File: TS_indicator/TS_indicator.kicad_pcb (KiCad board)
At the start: 2 copper layers, 140 x 60 mm, 50 parts, among them J1 Conn_01x02_Pin, J2 Conn_01x02_Pin, J3 Conn_01x02_Pin, J4 Conn_01x02_Pin, Q1 AO3401A, Q2 AO3400A, U1 TLV431, U2 PV15-27B12R3, U3 B1212, U7 LTV-817S

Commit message: added TS indicator
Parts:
- F1: footprint Fuse:Fuse_Littelfuse-NANO2-885 -> Fuse:Fuse_Littelfuse-NANO2-462
- moved R9 7.56 mm to (17.4, 36.1)
- moved R8 6.62 mm to (23.5, 36.0)
- moved R7 5.92 mm to (29.5, 35.9)
- moved R6 5.20 mm to (34.4, 37.2), turned to -90 degrees
- moved R10 4.31 mm to (26.2, 44.3), turned to 90 degrees
- moved C1 3.96 mm to (22.6, 52.1)
- moved C2 3.96 mm to (30.6, 49.6)
- moved C3 3.96 mm to (32.4, 63.8)
- moved D1 3.96 mm to (18.0, 47.5)
- moved LM1 3.96 mm to (30.5, 56.2)
- moved R1 3.96 mm to (22.8, 61.0)
- moved R11 3.96 mm to (26.4, 51.0)
- moved R12 3.96 mm to (35.0, 51.3)
- moved R2 3.96 mm to (22.8, 58.5)
- moved R4 3.96 mm to (22.9, 63.6)
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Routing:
- net /Vin: track 23.6 -> 34.5 mm
- net Net-(LM1-+): track 6.23 -> 11.5 mm
- net Net-(LM1-Pad7): track 86.8 -> 83.4 mm
- net Net-(R5-Pad2): track 2.54 -> 5.81 mm
- net /+HV_after_fuse: track 40.1 -> 42.5 mm
- net +12V: track 85.0 -> 83.2 mm
- net Net-(R3-Pad2): track 2.22 -> 3.88 mm
- net Net-(R8-Pad1): track 2.50 -> 3.94 mm
- net GND: track 231.3 -> 232.7 mm
- net /+HV: track 8.73 -> 10.1 mm
- net Net-(R6-Pad1): track 2.64 -> 3.87 mm
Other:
- outline, holes or cut-outs redrawn

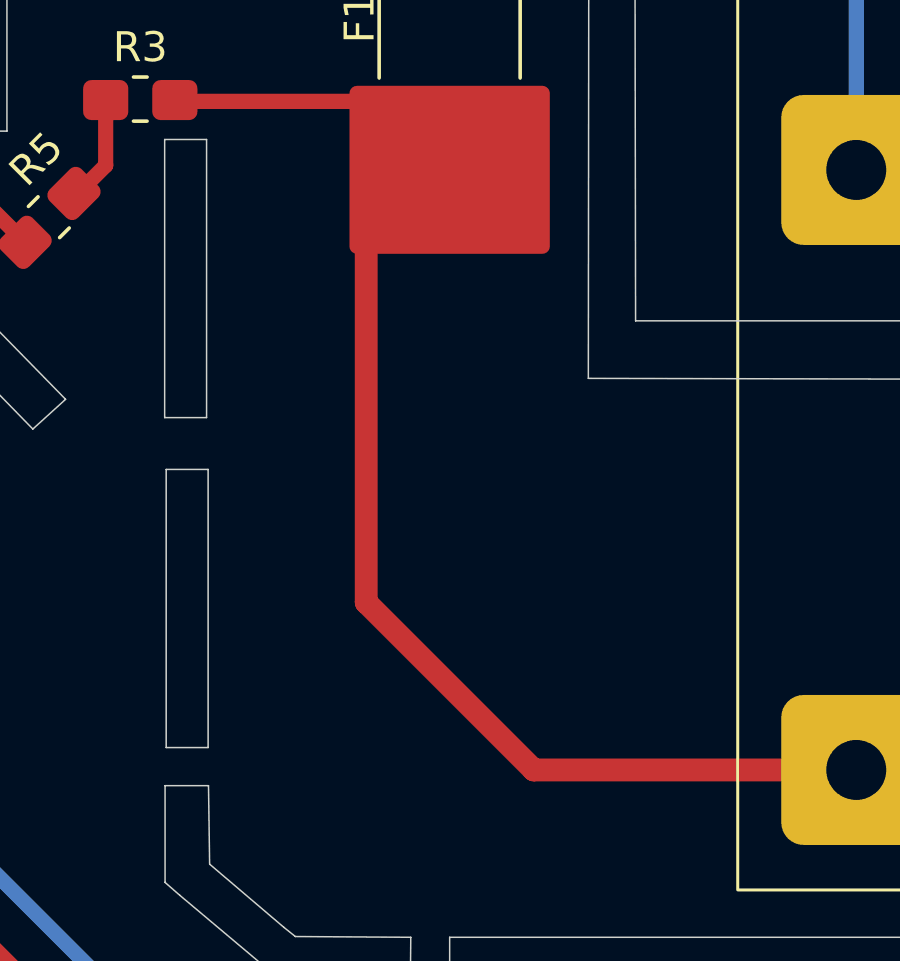
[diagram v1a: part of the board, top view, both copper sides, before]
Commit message: minor fix on TS indicator
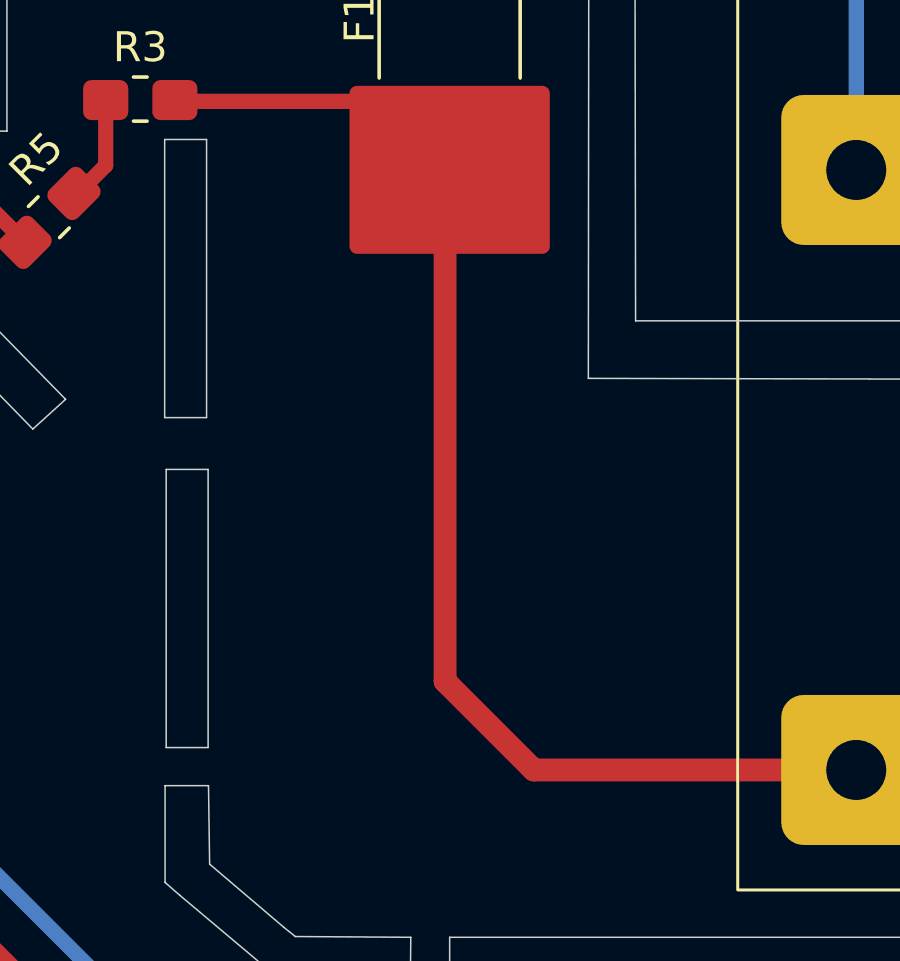
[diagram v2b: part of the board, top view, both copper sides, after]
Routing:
- net /+HV_after_fuse: track 42.5 -> 44.0 mm
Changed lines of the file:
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@@
-	)
-	(segment
-		(start 49.5173 54.6481)
-		(end 55.1028 60.2336)
-		(width 0.762)
-		(layer "F.Cu")
-		(net 29)
 	)
 	(segment
@@
 	)
 	(segment
-		(start 49.5173 40.9493)
-		(end 49.5173 54.6481)
+		(start 52.1462 57.277)
+		(end 55.1028 60.2336)
+		(width 0.762)
+		(layer "F.Cu")
+		(net 29)
+	)
+	(segment
+		(start 52.1462 40.9493)
+		(end 52.1462 57.277)
 		(width 0.762)
 		(layer "F.Cu")
@@
 		(width 0.762)
 		(layer "F.Cu")
+		(net 29)
+	)
+	(segment
+		(start 49.5173 40.9493)
+		(end 52.1462 40.9493)
+		(width 0.762)
+		(layer "F.Cu")

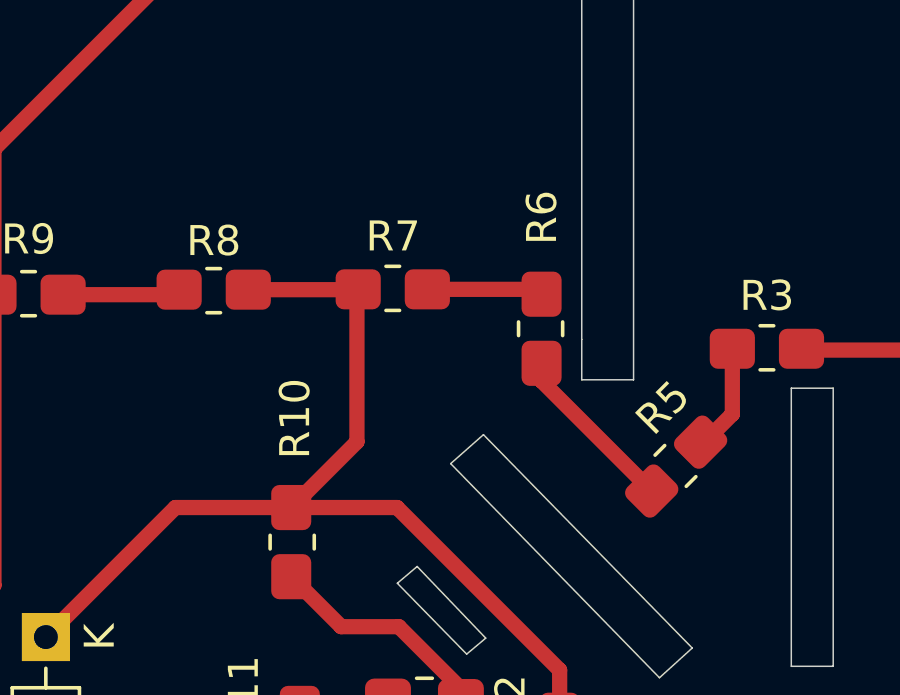
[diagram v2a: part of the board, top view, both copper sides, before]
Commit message: minor fix on TS indicator
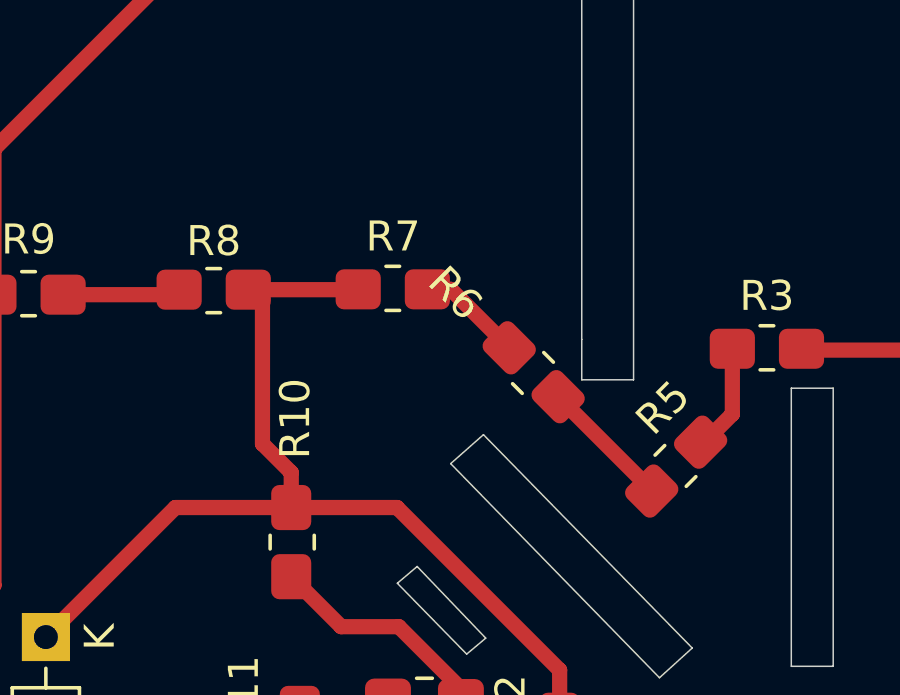
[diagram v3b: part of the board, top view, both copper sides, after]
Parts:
- moved R6 1.49 mm to (34.2, 38.7), turned to -45 degrees
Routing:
- net Net-(R5-Pad2): track 5.81 -> 4.47 mm
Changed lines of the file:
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@@
 	(footprint "RMC-KiCad:R_0805_2012Metric_Pad1.20x1.40mm_HandSolder_L"
 		(layer "F.Cu")
-		(at 34.4424 37.2364 -90)
+		(at 34.1884 38.7096 -45)
 		(descr "Resistor SMD 0805 (2012 Metric), square (rectangular) end terminal, IPC_7351 nominal with elongated pad for handsoldering. (Body size source: IPC-SM-782 page 72, https://www.pcb-3d.com/wordpress/wp-content/uploads/ipc-sm-782a_amendment_1_and_2.pdf), generated with kicad-footprint-generator")
 		(tags "resistor handsolder")
 		(property "Reference" "R6"
-			(at -3.7084 -0.0508 90)
+			(at -3.7084 -0.0508 135)
 			(layer "F.SilkS")
 			(effects
@@
 		)
 		(property "Value" "249k"
-			(at 0 1.65 90)
+			(at 0 1.65 135)
 			(layer "F.Fab")
 			(effects
@@
 		)
 		(property "Datasheet" ""
-			(at 0 0 90)
+			(at 0 0 135)
 			(layer "F.Fab")
 			(hide yes)
@@
 		)
 		(property "Description" ""
-			(at 0 0 90)
+			(at 0 0 135)
 			(layer "F.Fab")
 			(hide yes)
@@
 		)
 		(fp_line
-			(start 2.1844 0.949999)
-			(end -2.20158 0.952103)
+			(start -2.205883 -0.949309)
+			(end 2.1844 -0.949999)
 			(stroke
 				(width 0.05)
@@
 		)
 		(fp_line
-			(start -2.205883 -0.949309)
-			(end 2.1844 -0.949999)
+			(start 2.1844 0.949999)
+			(end -2.20158 0.952103)
 			(stroke
 				(width 0.05)
@@
 		)
 		(fp_line
-			(start 1 0.625)
-			(end -1 0.625)
+			(start -1 -0.625)
+			(end 1 -0.625)
 			(stroke
 				(width 0.1)
@@
 		)
 		(fp_line
-			(start -1 -0.625)
-			(end 1 -0.625)
+			(start 1 0.625)
+			(end -1 0.625)
 			(stroke
 				(width 0.1)
@@
 		)
 		(fp_text user "${REFERENCE}"
-			(at 0 0 90)
+			(at 0 0 135)
 			(layer "F.Fab")
 			(effects
@@
 		)
 		(pad "1" smd roundrect
-			(at -1.152501 -0.0325 270)
+			(at -1.152501 -0.0325 315)
 			(size 1.505 1.335)
 			(layers "F.Cu" "F.Mask" "F.Paste")
@@
 		)
 		(pad "2" smd roundrect
-			(at 1.152501 -0.0325 270)
+			(at 1.152501 -0.0325 315)
 			(size 1.505 1.335)
 			(layers "F.Cu" "F.Mask" "F.Paste")
@@
 				(keep_text_aligned yes)
 			)
-			(gr_text "20"
+			(gr_text "787.4016"
 				(at 64.701 50.2336 90)
 				(layer "Dwgs.User")
@@
 				(keep_text_aligned yes)
 			)
-			(gr_text "3.95"
+			(gr_text "155.5118"
 				(at 129.926 63.0836 0)
 				(layer "Dwgs.User")
@@
 				(keep_text_aligned yes)
 			)
-			(gr_text "3.95"
+			(gr_text "155.5118"
 				(at 63.876 63.0836 0)
 				(layer "Dwgs.User")
@@
 				(keep_text_aligned yes)
 			)
-			(gr_text "23"
+			(gr_text "905.5118"
 				(at 126.801001 40.2336 90)
 				(layer "Dwgs.User")
@@
 				(keep_text_aligned yes)
 			)
-			(gr_text "12.5"
+			(gr_text "492.126"
 				(at 126.801 57.9836 90)
 				(layer "Dwgs.User")
@@
 				(keep_text_aligned yes)
 			)
-			(gr_text "4"
+			(gr_text "157.4803"
 				(at 64.701 62.2336 90)
 				(layer "Dwgs.User")
@@
 	(gr_line
 		(start 38.1 41.7322)
-		(end 35.179 36.5252)
+		(end 34.2646 38.0746)
 		(stroke
 			(width 0.1)
@@
 	)
 	(segment
+		(start 25.1714 36.407)
+		(end 24.6983 35.9339)
+		(width 0.508)
+		(layer "F.Cu")
+		(net 8)
+	)
+	(segment
 		(start 35.0774 48.6156)
 		(end 29.657699 43.195899)
@@
 	)
 	(segment
-		(start 28.321 41.004399)
-		(end 26.1295 43.195899)
+		(start 26.1295 42.0299)
+		(end 25.1714 41.0718)
+		(width 0.508)
+		(layer "F.Cu")
+		(net 8)
+	)
+	(segment
+		(start 26.1295 43.195899)
+		(end 26.1295 42.0299)
 		(width 0.508)
 		(layer "F.Cu")
@@
 	)
 	(segment
-		(start 28.321 35.963999)
-		(end 28.321 41.004399)
+		(start 25.1714 41.0718)
+		(end 25.1714 36.407)
 		(width 0.508)
 		(layer "F.Cu")
@@
 	)
 	(segment
-		(start 34.4749 38.974982)
-		(end 38.14624 42.646322)
+		(start 38.14624 42.621478)
+		(end 35.026322 39.50156)
 		(width 0.508)
 		(layer "F.Cu")
@@
 	)
 	(segment
-		(start 34.4749 38.388901)
-		(end 34.4749 38.974982)
-		(width 0.508)
+		(start 38.337398 42.056002)
+		(end 38.3127 42.0807)
+		(width 0.2)
 		(layer "F.Cu")
 		(net 24)
 	)
 	(segment
-		(start 38.337398 42.056002)
-		(end 38.3127 42.0807)
-		(width 0.2)
+		(start 38.14624 42.646322)
+		(end 38.14624 42.621478)
+		(width 0.508)
 		(layer "F.Cu")
 		(net 24)
 	)
 	(segment
-		(start 30.667301 35.9227)
-		(end 34.313701 35.9227)
+		(start 33.39644 37.871678)
+		(end 31.447462 35.9227)
 		(width 0.508)
 		(layer "F.Cu")
@@
 	)
 	(segment
-		(start 34.313701 35.9227)
-		(end 34.4749 36.083899)
-		(width 0.2)
+		(start 31.447462 35.9227)
+		(end 30.667301 35.9227)
+		(width 0.508)
 		(layer "F.Cu")
 		(net 25)

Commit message: minor update on TS side
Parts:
- moved R6 0.57 mm to (34.1, 39.3)
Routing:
- net Net-(R6-Pad1): track 3.54 -> 4.05 mm
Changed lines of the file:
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@@
 	(footprint "RMC-KiCad:R_0805_2012Metric_Pad1.20x1.40mm_HandSolder_L"
 		(layer "F.Cu")
-		(at 34.1884 38.7096 -45)
+		(at 34.0868 39.2684 -45)
 		(descr "Resistor SMD 0805 (2012 Metric), square (rectangular) end terminal, IPC_7351 nominal with elongated pad for handsoldering. (Body size source: IPC-SM-782 page 72, https://www.pcb-3d.com/wordpress/wp-content/uploads/ipc-sm-782a_amendment_1_and_2.pdf), generated with kicad-footprint-generator")
 		(tags "resistor handsolder")
 		(property "Reference" "R6"
-			(at -3.7084 -0.0508 135)
+			(at -2.155261 1.76013 135)
 			(layer "F.SilkS")
 			(effects
@@
 				(keep_text_aligned yes)
 			)
-			(gr_text "787.4016"
+			(gr_text "20"
 				(at 64.701 50.2336 90)
 				(layer "Dwgs.User")
@@
 				(keep_text_aligned yes)
 			)
-			(gr_text "155.5118"
+			(gr_text "3.95"
 				(at 129.926 63.0836 0)
 				(layer "Dwgs.User")
@@
 				(keep_text_aligned yes)
 			)
-			(gr_text "155.5118"
+			(gr_text "3.95"
 				(at 63.876 63.0836 0)
 				(layer "Dwgs.User")
@@
 				(keep_text_aligned yes)
 			)
-			(gr_text "905.5118"
+			(gr_text "23"
 				(at 126.801001 40.2336 90)
 				(layer "Dwgs.User")
@@
 				(keep_text_aligned yes)
 			)
-			(gr_text "492.126"
+			(gr_text "12.5"
 				(at 126.801 57.9836 90)
 				(layer "Dwgs.User")
@@
 				(keep_text_aligned yes)
 			)
-			(gr_text "157.4803"
+			(gr_text "4"
 				(at 64.701 62.2336 90)
 				(layer "Dwgs.User")
@@
 	)
 	(gr_line
+		(start 32.4358 38.2524)
+		(end 29.0576 36.5506)
+		(stroke
+			(width 0.1)
+			(type default)
+		)
+		(layer "Dwgs.User")
+	)
+	(gr_line
 		(start 32.7406 45.7962)
 		(end 37.3888 42.926)
 		(stroke
 			(width 0.1)
-			(type default)
+			(type solid)
 		)
 		(layer "Dwgs.User")
@@
 	)
 	(gr_line
-		(start 38.1 41.7322)
-		(end 34.2646 38.0746)
+		(start 33.274 39.2684)
+		(end 29.845 43.0022)
 		(stroke
 			(width 0.1)
@@
 	)
 	(gr_line
+		(start 38.1 41.7322)
+		(end 33.821635 38.119351)
+		(stroke
+			(width 0.1)
+			(type solid)
+		)
+		(layer "Dwgs.User")
+	)
+	(gr_line
 		(start 40.1066 38.3032)
 		(end 38.1 41.7322)
 		(stroke
 			(width 0.1)
-			(type default)
+			(type solid)
 		)
 		(layer "Dwgs.User")
@@
 	)
 	(segment
-		(start 38.14624 42.621478)
-		(end 35.026322 39.50156)
+		(start 38.14624 42.646322)
+		(end 37.510684 42.646322)
 		(width 0.508)
 		(layer "F.Cu")
@@
 	)
 	(segment
-		(start 38.14624 42.646322)
-		(end 38.14624 42.621478)
+		(start 37.510684 42.646322)
+		(end 35.026322 40.16196)
 		(width 0.508)
 		(layer "F.Cu")
@@
 	)
 	(segment
-		(start 33.39644 37.871678)
-		(end 31.447462 35.9227)
+		(start 33.29484 38.430478)
+		(end 33.29484 37.770078)
 		(width 0.508)
 		(layer "F.Cu")
@@
 		(width 0.508)
 		(layer "F.Cu")
+		(net 25)
+	)
+	(segment
+		(start 33.29484 37.770078)
+		(end 31.447462 35.9227)
+		(width 0.508)
+		(layer "F.Cu")

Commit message: minor adjustment on TS
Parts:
- moved R3 1.36 mm to (43.3, 38.1)
- moved R7 0.98 mm to (30.0, 35.0), turned to 135 degrees
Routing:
- net /Vin: track 34.2 -> 36.6 mm
- net /+HV_after_fuse: track 44.0 -> 42.7 mm
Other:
- outline, holes or cut-outs redrawn
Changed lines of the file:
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@@
 	(footprint "RMC-KiCad:R_0805_2012Metric_Pad1.20x1.40mm_HandSolder_L"
 		(layer "F.Cu")
-		(at 41.9862 37.8714 180)
+		(at 43.3324 38.0746 180)
 		(descr "Resistor SMD 0805 (2012 Metric), square (rectangular) end terminal, IPC_7351 nominal with elongated pad for handsoldering. (Body size source: IPC-SM-782 page 72, https://www.pcb-3d.com/wordpress/wp-content/uploads/ipc-sm-782a_amendment_1_and_2.pdf), generated with kicad-footprint-generator")
 		(tags "resistor handsolder")
@@
 	(footprint "RMC-KiCad:R_0805_2012Metric_Pad1.20x1.40mm_HandSolder_L"
 		(layer "F.Cu")
-		(at 29.5148 35.8902 180)
+		(at 29.972 35.0266 135)
 		(descr "Resistor SMD 0805 (2012 Metric), square (rectangular) end terminal, IPC_7351 nominal with elongated pad for handsoldering. (Body size source: IPC-SM-782 page 72, https://www.pcb-3d.com/wordpress/wp-content/uploads/ipc-sm-782a_amendment_1_and_2.pdf), generated with kicad-footprint-generator")
 		(tags "resistor handsolder")
 		(property "Reference" "R7"
-			(at -0.010742 1.7272 0)
+			(at -0.010742 1.7272 135)
 			(layer "F.SilkS")
 			(effects
@@
 		)
 		(property "Value" "249k"
-			(at 0 1.65 0)
+			(at 0 1.65 135)
 			(layer "F.Fab")
 			(effects
@@
 		)
 		(property "Datasheet" ""
-			(at 0 0 0)
+			(at 0 0 135)
 			(layer "F.Fab")
 			(hide yes)
@@
 		)
 		(property "Description" ""
-			(at 0 0 0)
+			(at 0 0 135)
 			(layer "F.Fab")
 			(hide yes)
@@
 		(attr smd)
 		(fp_line
-			(start -0.227064 0.735)
-			(end 0.227064 0.735)
+			(start -0.227064 -0.735)
+			(end 0.227064 -0.735)
 			(stroke
 				(width 0.12)
@@
 		)
 		(fp_line
-			(start -0.227064 -0.735)
-			(end 0.227064 -0.735)
+			(start -0.227064 0.735)
+			(end 0.227064 0.735)
 			(stroke
 				(width 0.12)
@@
 		)
 		(fp_line
-			(start 2.1844 0.949999)
-			(end -2.20158 0.952103)
+			(start 2.1844 -0.949999)
+			(end 2.1844 0.949999)
 			(stroke
 				(width 0.05)
@@
 		)
 		(fp_line
-			(start 2.1844 -0.949999)
-			(end 2.1844 0.949999)
+			(start 2.1844 0.949999)
+			(end -2.20158 0.952103)
 			(stroke
 				(width 0.05)
@@
 		)
 		(fp_line
-			(start -2.20158 0.952103)
-			(end -2.205883 -0.949309)
+			(start -2.205883 -0.949309)
+			(end 2.1844 -0.949999)
 			(stroke
 				(width 0.05)
@@
 		)
 		(fp_line
-			(start -2.205883 -0.949309)
-			(end 2.1844 -0.949999)
+			(start -2.20158 0.952103)
+			(end -2.205883 -0.949309)
 			(stroke
 				(width 0.05)
@@
 		)
 		(fp_line
-			(start 1 0.625)
-			(end -1 0.625)
+			(start 1 -0.625)
+			(end 1 0.625)
 			(stroke
 				(width 0.1)
@@
 		)
 		(fp_line
-			(start 1 -0.625)
-			(end 1 0.625)
+			(start 1 0.625)
+			(end -1 0.625)
 			(stroke
 				(width 0.1)
@@
 		)
 		(fp_line
-			(start -1 0.625)
-			(end -1 -0.625)
+			(start -1 -0.625)
+			(end 1 -0.625)
 			(stroke
 				(width 0.1)
@@
 		)
 		(fp_line
-			(start -1 -0.625)
-			(end 1 -0.625)
+			(start -1 0.625)
+			(end -1 -0.625)
 			(stroke
 				(width 0.1)
@@
 		)
 		(fp_text user "${REFERENCE}"
-			(at 0 0 0)
+			(at 0 0 135)
 			(layer "F.Fab")
 			(effects
@@
 		)
 		(pad "1" smd roundrect
-			(at -1.152501 -0.0325 180)
+			(at -1.152501 -0.0325 135)
 			(size 1.505 1.335)
 			(layers "F.Cu" "F.Mask" "F.Paste")
@@
 		)
 		(pad "2" smd roundrect
-			(at 1.152501 -0.0325 180)
+			(at 1.152501 -0.0325 135)
 			(size 1.505 1.335)
 			(layers "F.Cu" "F.Mask" "F.Paste")
@@
 	)
 	(gr_line
-		(start 43.7896 37.2364)
+		(start 45.1104 37.4496)
 		(end 48.9966 32.8422)
 		(stroke
@@
 	)
 	(gr_line
-		(start 32.4358 38.2524)
-		(end 29.0576 36.5506)
-		(stroke
-			(width 0.1)
-			(type default)
-		)
-		(layer "Dwgs.User")
-	)
-	(gr_line
 		(start 32.7406 45.7962)
 		(end 37.3888 42.926)
@@
 	)
 	(gr_line
-		(start 38.1 41.7322)
+		(start 37.973 41.8592)
 		(end 33.821635 38.119351)
 		(stroke
@@
 	)
 	(gr_line
-		(start 40.1066 38.3032)
-		(end 38.1 41.7322)
-		(stroke
-			(width 0.1)
-			(type solid)
-		)
-		(layer "Dwgs.User")
-	)
-	(gr_line
 		(start 39.497 47.879)
 		(end 32.5374 40.767)
@@
 	)
 	(gr_rect
-		(start 42.799 39.2176)
+		(start 42.799 39.578892)
 		(end 44.196 48.4886)
 		(stroke
@@
 	)
 	(segment
-		(start 28.362299 35.9227)
-		(end 28.321 35.963999)
+		(start 25.73476 33.92984)
+		(end 29.362678 33.92984)
+		(width 0.508)
+		(layer "F.Cu")
+		(net 8)
+	)
+	(segment
+		(start 24.6983 34.9663)
+		(end 25.73476 33.92984)
+		(width 0.508)
+		(layer "F.Cu")
+		(net 8)
+	)
+	(segment
+		(start 24.6983 35.9339)
+		(end 24.6983 34.9663)
 		(width 0.508)
 		(layer "F.Cu")
@@
 	)
 	(segment
-		(start 28.351099 35.9339)
-		(end 28.362299 35.9227)
-		(width 0.2)
-		(layer "F.Cu")
-		(net 8)
-	)
-	(segment
-		(start 24.6983 35.9339)
-		(end 28.351099 35.9339)
-		(width 0.508)
-		(layer "F.Cu")
-		(net 8)
-	)
-	(segment
 		(start 22.2687 43.195899)
 		(end 17.9507 47.513899)
@@
 	)
 	(segment
-		(start 40.833699 37.9039)
-		(end 40.833699 40.081902)
+		(start 42.179899 38.1071)
+		(end 42.179899 38.735702)
 		(width 0.508)
 		(layer "F.Cu")
@@
 	)
 	(segment
-		(start 40.833699 40.081902)
+		(start 42.179899 38.735702)
 		(end 39.633501 41.2821)
 		(width 0.508)
@@
 	(segment
 		(start 33.29484 38.430478)
-		(end 33.29484 37.770078)
+		(end 33.29484 38.34944)
 		(width 0.508)
 		(layer "F.Cu")
@@
 	)
 	(segment
-		(start 31.447462 35.9227)
-		(end 30.667301 35.9227)
+		(start 30.99256 36.04716)
+		(end 30.99256 35.559722)
 		(width 0.508)
 		(layer "F.Cu")
@@
 	)
 	(segment
-		(start 33.29484 37.770078)
-		(end 31.447462 35.9227)
+		(start 33.29484 38.34944)
+		(end 30.99256 36.04716)
 		(width 0.508)
 		(layer "F.Cu")
@@
 	)
 	(segment
-		(start 52.2986 40.229)
-		(end 50.0172 37.9476)
-		(width 0.508)
-		(layer "F.Cu")
-		(net 29)
-	)
-	(segment
-		(start 43.182401 37.9476)
-		(end 43.138701 37.9039)
-		(width 0.508)
-		(layer "F.Cu")
-		(net 29)
-	)
-	(segment
-		(start 50.0172 37.9476)
-		(end 43.182401 37.9476)
+		(start 44.644401 37.9476)
+		(end 44.484901 38.1071)
 		(width 0.508)
 		(layer "F.Cu")
@@
 	)
 	(segment
+		(start 52.2986 40.229)
+		(end 50.0172 37.9476)
+		(width 0.508)
+		(layer "F.Cu")
+		(net 29)
+	)
+	(segment
 		(start 55.1028 60.2336)
 		(end 65.851 60.2336)
@@
 		(layer "F.Cu")
 		(net 29)
+	)
+	(segment
+		(start 50.0172 37.9476)
+		(end 44.644401 37.9476)
+		(width 0.508)
+		(layer "F.Cu")
+		(net 29)

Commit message: minor adjustment on GLV
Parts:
- D3, D4: moved to F.Cu
- moved D3 3.00 mm to (135.4, 34.7)
- moved R22 3.00 mm to (140.5, 34.8)
- moved R18 3.00 mm to (138.0, 34.8)
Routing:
- net Net-(J3-Pin_1): track 7.82 -> 4.86 mm
- net VCC: track 79.6 -> 82.1 mm
- net Net-(D3-K): track 17.3 -> 17.4 mm, vias 0 -> 1
- net Net-(D3-A): vias 0 -> 1
- net Net-(D4-A): vias 0 -> 1
- net /GLV-: vias 26 -> 27
